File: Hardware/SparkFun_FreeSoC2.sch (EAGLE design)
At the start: 109 parts, among them U1 CY8C5888AXI-LP096, U2 MIC5219 5V, U3 MIC5219 3.3V, U4 2A/20V, U7 CY8C5868LTI-LP039, Y1 32.768kHz

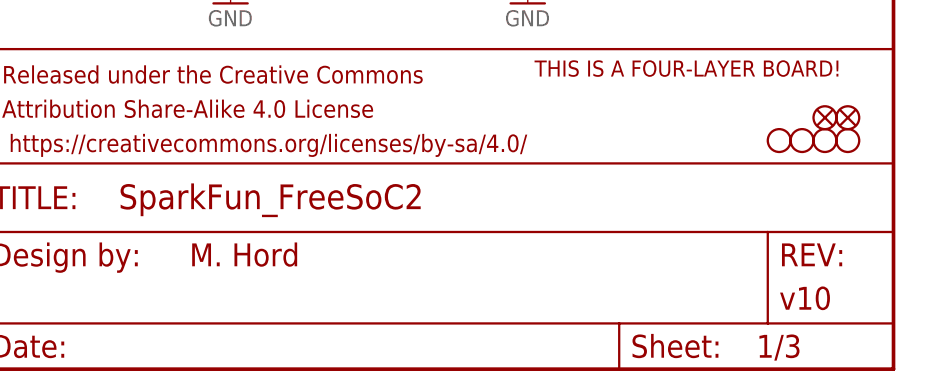
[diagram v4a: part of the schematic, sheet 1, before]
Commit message: Rev to 11 to fix rev #, layers issue
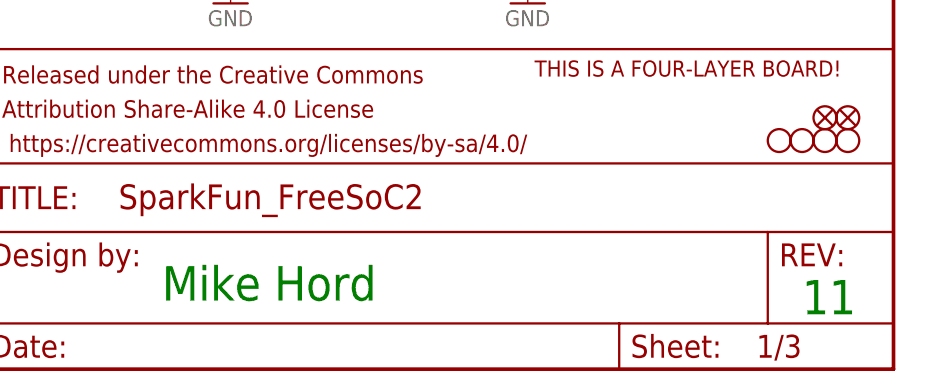
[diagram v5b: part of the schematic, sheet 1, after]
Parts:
- FRAME1, FRAME2, FRAME3: device SparkFun-Aesthetics:FRAME-LETTER -> SparkFun-Aesthetics:FRAME-LETTERNO_PACKAGE; DESIGNER M. Hord -> (none); VERSION v10 -> (none)
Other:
- note added: "11"
- note added: "Mike Hord"
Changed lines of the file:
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@@
 </classes>
 <parts>
-<part name="FRAME1" library="SparkFun-Aesthetics" deviceset="FRAME-LETTER" device="">
-<attribute name="DESIGNER" value="M. Hord"/>
-<attribute name="VERSION" value="v10"/>
-</part>
 <part name="U1" library="SparkFun-DigitalIC" deviceset="PSOC_5LP_100QFP" device="" value="CY8C5888AXI-LP096"/>
 <part name="D1" library="SparkFun-DiscreteSemi" deviceset="MBRA140" device=""/>
 <part name="D2" library="SparkFun-DiscreteSemi" deviceset="MBRA140" device=""/>
 <part name="D3" library="SparkFun-DiscreteSemi" deviceset="MBRA140" device=""/>
-<part name="FRAME2" library="SparkFun-Aesthetics" deviceset="FRAME-LETTER" device="">
-<attribute name="DESIGNER" value="M. Hord"/>
-<attribute name="VERSION" value="v10"/>
-</part>
 <part name="JP3" library="SparkFun-Connectors" deviceset="M02" device="JST-PTH-2"/>
 <part name="JP18" library="SparkFun-Connectors" deviceset="POWER_JACK" device="PTH_LOCK" value="POWER_JACKPTH_LOCK"/>
@@
 <part name="GND32" library="SparkFun-Aesthetics" deviceset="GND" device=""/>
 <part name="D4" library="SparkFun-DiscreteSemi" deviceset="MBRA140" device=""/>
-<part name="FRAME3" library="SparkFun-Aesthetics" deviceset="FRAME-LETTER" device="">
-<attribute name="DESIGNER" value="M. Hord"/>
-<attribute name="VERSION" value="v10"/>
-</part>
 <part name="U7" library="SparkFun-DigitalIC" deviceset="PSOC_5LP_68QFN" device="" value="CY8C5868LTI-LP039"/>
 <part name="GND33" library="SparkFun-Aesthetics" deviceset="GND" device=""/>
@@
 <part name="SJ6" library="SparkFun-Passives" deviceset="JUMPER-PAD-2-NO" device=""/>
 <part name="SJ7" library="SparkFun-Passives" deviceset="JUMPER-PAD-2-NO" device=""/>
+<part name="FRAME1" library="SparkFun-Aesthetics" deviceset="FRAME-LETTER" device="NO_PACKAGE"/>
+<part name="FRAME2" library="SparkFun-Aesthetics" deviceset="FRAME-LETTER" device="NO_PACKAGE"/>
+<part name="FRAME3" library="SparkFun-Aesthetics" deviceset="FRAME-LETTER" device="NO_PACKAGE"/>
 </parts>
 <sheets>
@@
 <text x="166.116" y="115.316" size="1.778" layer="97">USER
 LED</text>
+<text x="167.64" y="7.62" size="3.81" layer="91">Mike Hord</text>
+<text x="238.76" y="6.096" size="3.81" layer="91">11</text>
 </plain>
 <instances>
-<instance part="FRAME1" gate="G$1" x="0" y="0"/>
-<instance part="FRAME1" gate="V" x="147.32" y="0"/>
 <instance part="U1" gate="G1" x="7.62" y="129.54"/>
 <instance part="U1" gate="G2" x="7.62" y="40.64"/>
@@
 <instance part="LOGO1" gate="G$1" x="53.34" y="0"/>
 <instance part="LOGO2" gate="G$1" x="66.04" y="22.86"/>
+<instance part="FRAME3" gate="G$1" x="0" y="0"/>
+<instance part="FRAME3" gate="V" x="147.32" y="0"/>
 </instances>
 <busses>
@@
 battery operation</text>
 <text x="35.56" y="17.78" size="1.778" layer="97">JP3 is DNP</text>
+<text x="167.64" y="7.62" size="3.81" layer="91">Mike Hord</text>
+<text x="238.252" y="6.096" size="3.81" layer="91">11</text>
 </plain>
 <instances>
@@
 <instance part="D2" gate="G$1" x="76.2" y="73.66"/>
 <instance part="D3" gate="G$1" x="60.96" y="43.18"/>
-<instance part="FRAME2" gate="G$1" x="0" y="0"/>
-<instance part="FRAME2" gate="V" x="147.32" y="0"/>
 <instance part="U1" gate="G5" x="27.94" y="127"/>
 <instance part="JP3" gate="G$1" x="40.64" y="25.4"/>
@@
 <instance part="GND41" gate="1" x="218.44" y="53.34"/>
 <instance part="GND43" gate="1" x="182.88" y="43.18"/>
+<instance part="FRAME2" gate="G$1" x="0" y="0"/>
+<instance part="FRAME2" gate="V" x="147.32" y="0"/>
 </instances>
 <busses>
@@
 Close to connect debugger
 to target via I2C</text>
+<text x="167.64" y="7.62" size="3.81" layer="91">Mike Hord</text>
+<text x="237.744" y="6.35" size="3.81" layer="91">11</text>
 </plain>
 <instances>
-<instance part="FRAME3" gate="G$1" x="0" y="0"/>
-<instance part="FRAME3" gate="V" x="147.32" y="0"/>
 <instance part="U7" gate="G1" x="5.08" y="147.32"/>
 <instance part="U7" gate="G2" x="73.66" y="147.32"/>
@@
 <attribute name="NAME" x="9.906" y="56.642" size="1.778" layer="95"/>
 </instance>
+<instance part="FRAME1" gate="G$1" x="0" y="0"/>
+<instance part="FRAME1" gate="V" x="147.32" y="0"/>
 </instances>
 <busses>

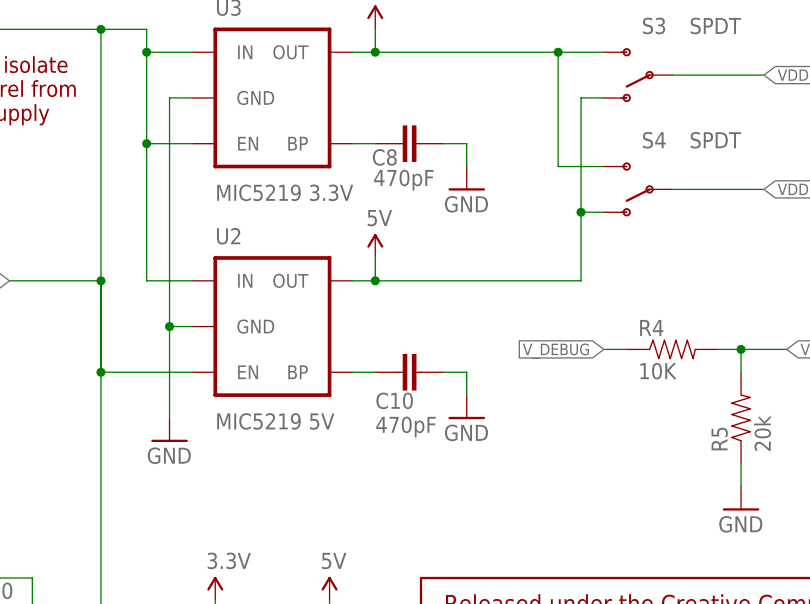
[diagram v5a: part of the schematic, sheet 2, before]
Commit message: Changed value of DNP caps to DNP
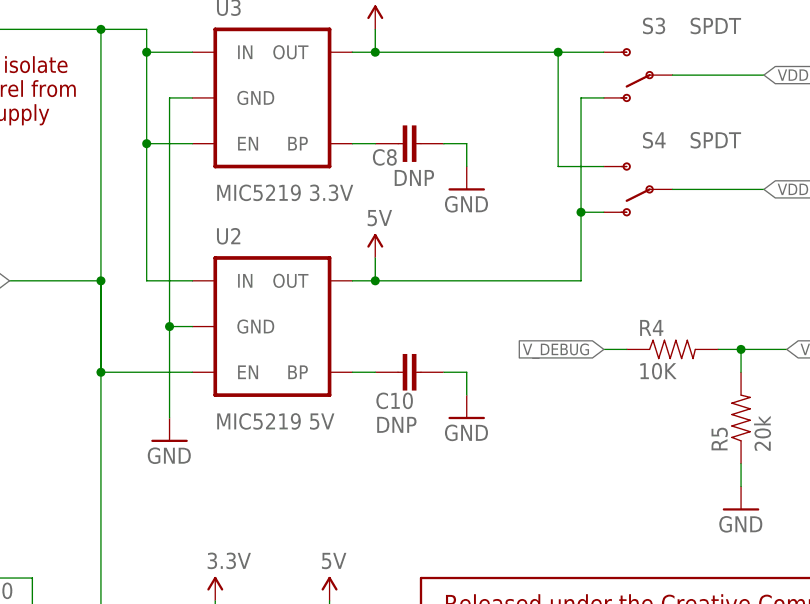
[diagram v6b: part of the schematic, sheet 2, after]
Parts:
- C10, C8: value 470pF -> DNP
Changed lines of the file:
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@@
 <?xml version="1.0" encoding="utf-8"?>
 <!DOCTYPE eagle SYSTEM "eagle.dtd">
-<eagle version="7.1.0">
+<eagle version="7.4.0">
 <drawing>
 <settings>
@@
 <part name="U3" library="SparkFun-PowerIC" deviceset="V_REG_MIC5219" device="3.3V" value="MIC5219 3.3V"/>
 <part name="GND1" library="SparkFun-Aesthetics" deviceset="GND" device=""/>
-<part name="C8" library="SparkFun-Capacitors" deviceset="470PF-50V-5%(0603)" device="SMD" value="470pF"/>
-<part name="C10" library="SparkFun-Capacitors" deviceset="470PF-50V-5%(0603)" device="SMD" value="470pF"/>
+<part name="C8" library="SparkFun-Capacitors" deviceset="470PF-50V-5%(0603)" device="SMD" value="DNP"/>
+<part name="C10" library="SparkFun-Capacitors" deviceset="470PF-50V-5%(0603)" device="SMD" value="DNP"/>
 <part name="GND2" library="SparkFun-Aesthetics" deviceset="GND" device=""/>
 <part name="GND3" library="SparkFun-Aesthetics" deviceset="GND" device=""/>
